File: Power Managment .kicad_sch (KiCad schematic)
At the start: 11 parts, among them J1 Main_12+, U2 AMS1117-3.3

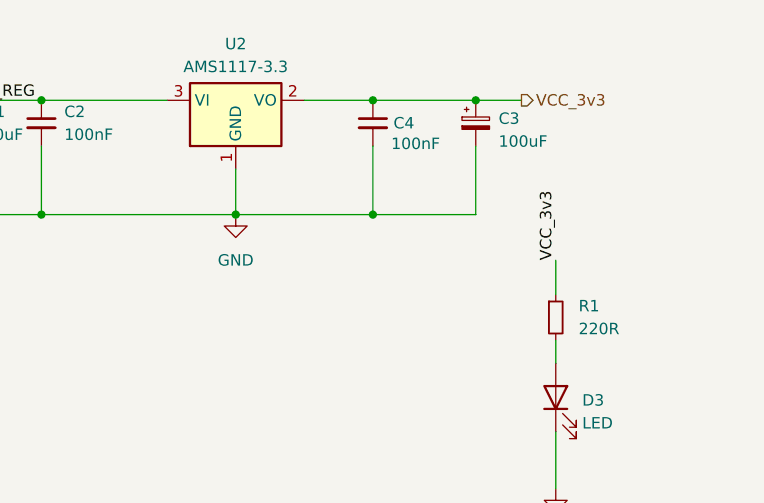
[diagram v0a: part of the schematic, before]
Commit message: updated Routing
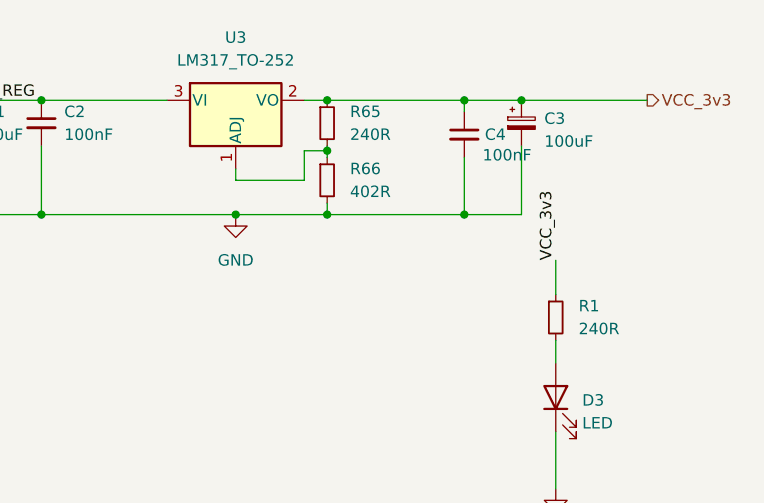
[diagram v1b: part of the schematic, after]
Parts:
- removed U2: AMS1117-3.3, Package_TO_SOT_SMD:SOT-223-3_TabPin2, symbol Regulator_Linear:AMS1117-3.3
- added R65: 240R, Resistor_SMD:R_0603_1608Metric, symbol Device:R_Small
- added R66: 402R, Resistor_SMD:R_0603_1608Metric, symbol Device:R_Small
- added U3: LM317_TO-252, Package_TO_SOT_SMD:TO-252-2, symbol Regulator_Linear:LM317_TO-252
- C1, C2, C4: footprint (none) -> Capacitor_SMD:C_0603_1608Metric
- C3: footprint (none) -> Capacitor_THT:CP_Radial_D6.3mm_P2.50mm
- D3: footprint (none) -> LED_SMD:LED_0603_1608Metric
- J1: footprint (none) -> TerminalBlock_Phoenix:TerminalBlock_Phoenix_MKDS-3-2-5.08_1x02_P5.08mm_Horizontal
- R1: value 220R -> 240R; footprint (none) -> Resistor_SMD:R_0603_1608Metric
- TH1: footprint (none) -> Fuse:Fuse_1812_4532Metric
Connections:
- net GND: now also R66.2
- net VCC_3v3: now also R65.1, U3.2 (VO)
- net Vcc_12_REG: now also U3.3 (VI)
- new net: R65.2, R66.1, U3.1 (ADJ)
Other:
- moved on the sheet: C3, C4
